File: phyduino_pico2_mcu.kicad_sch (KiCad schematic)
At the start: 68 parts, among them J1 1.0-3PWT, SW1 1977067-1, SW2 MINI MSK12CO2, U1 RP2350B, U2 GD25LQ128EWIGR, U3 PCA9570GMH, U4 XC6190AN157R-G, U5 ADS7038QRTERQ1, U7 ZD24C64A-MAGMT, Y1 XC32M4-12.000-F10NNFT

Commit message: nigthly commit
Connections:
- net unconnected-(SW2-MountPin-PadMP)_2: no longer names the net of SW2.MP (MountPin)
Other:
- company: (none) -> University of Toronto, Dept. of Physics
- title: (none) -> Phyduino Pico 2
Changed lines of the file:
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@@
 	(generator_version "10.0")
 	(paper "B")
+	(title_block
+		(title "Phyduino Pico 2")
+		(date "2026-05-04")
+		(rev "A")
+		(company "University of Toronto, Dept. of Physics")
+	)
 	(text "UART1"
 		(exclude_from_sim no)
@@
 			)
 			(justify right bottom)
-		)
-	)
-	(label "unconnected-(SW2-MountPin-PadMP)_2"
-		(at 36.83 118.11 270)
-		(effects
-			(font
-				(size 1.27 1.27)
-			)
-			(justify right bottom)

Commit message: Made schematic changes : merged usb_pd sheet with wifi sheet. made system regulators adjustable.
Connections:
- net BUILTIN_LED: now also U1.47 (GPIO38); no longer U1.43 (GPIO34)
- net D0: now also U1.44 (GPIO35); no longer U1.78 (GPIO1)
- net D1: now also U1.43 (GPIO34); no longer U1.77 (GPIO0)
- net D18 renamed D14
- net D19 renamed D15
- net WIFI_UART_SEL: no longer names the net of U1.3 (GPIO6)
- new net WIFI_DL_UART_RX: U1.78 (GPIO1)
- new net WIFI_DL_UART_TX: U1.77 (GPIO0)
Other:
- note added: "D0/UART_RX"
- note added: "D1/UART_TX"
- note added: "D14/I^{2}C_SDA"
- note added: "D15/I^{2}C_SCL"
- note added: "External Analog-to-Digital Converter"
- note added: "I^{2}C Addr = 0x48"
- note added: "I^{2}C Addr = 0x70"
- note added: "Microcontroller"
- note added: "Power Indicators & EEPROM"
- moved on the sheet: C1, C10, C11, C110, C111, C117, C119, C12, C120, C125, C126, C129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

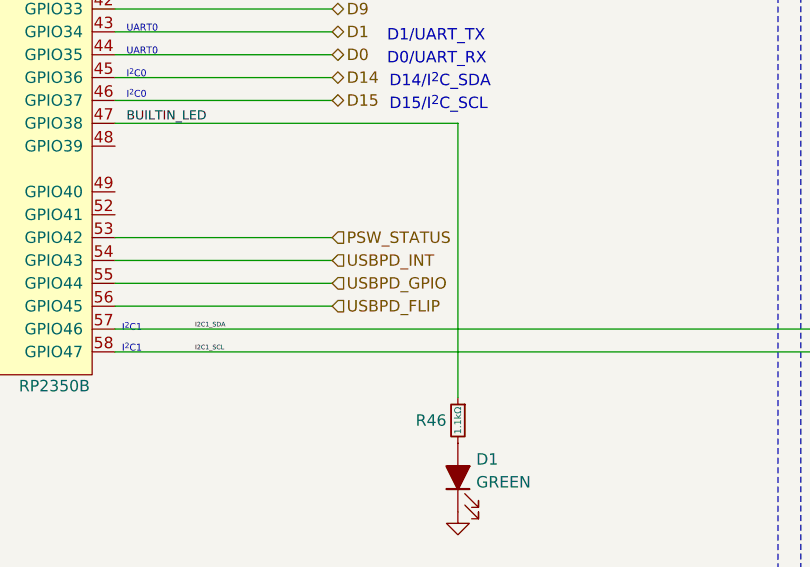
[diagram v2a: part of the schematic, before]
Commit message: Made changes to the power tree to allow +Vin to power the board.
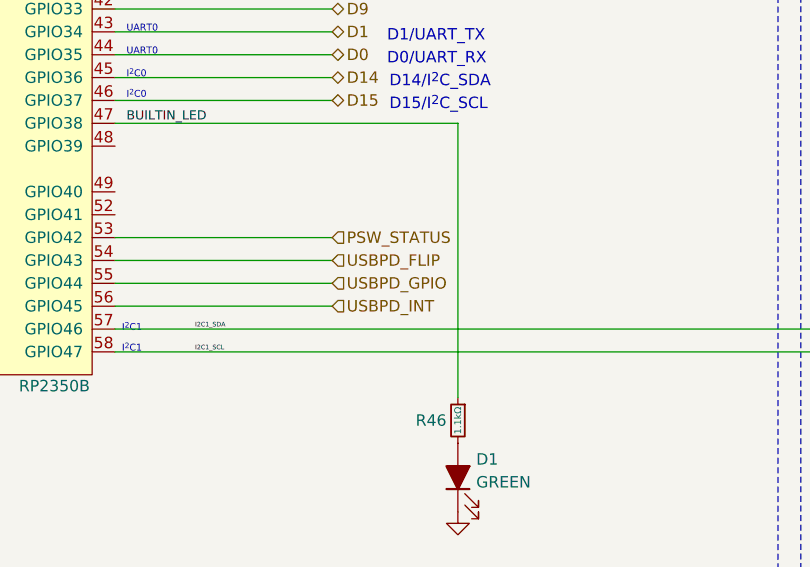
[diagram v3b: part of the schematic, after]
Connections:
- net USBPD_FLIP: now also U1.54 (GPIO43); no longer U1.56 (GPIO45)
- net USBPD_INT: now also U1.56 (GPIO45); no longer U1.54 (GPIO43)
